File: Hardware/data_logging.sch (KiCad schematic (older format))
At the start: 8 parts, among them J5 DM3CS-SF, U7 W25Q128JVS

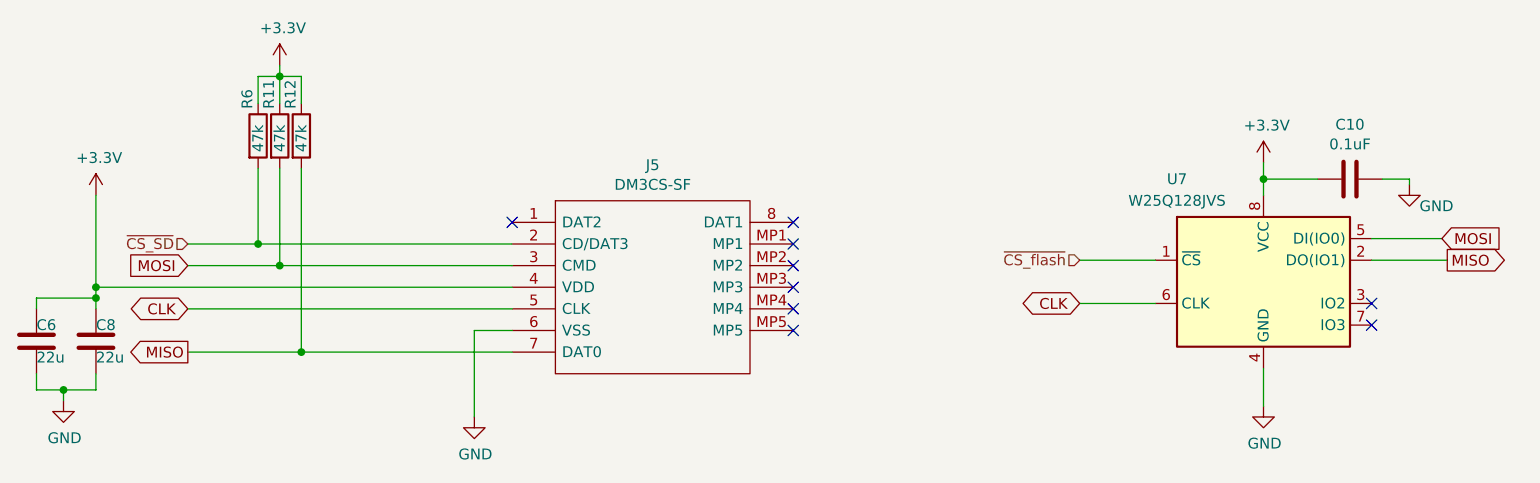
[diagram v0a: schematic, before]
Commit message: Update schematic, component placement
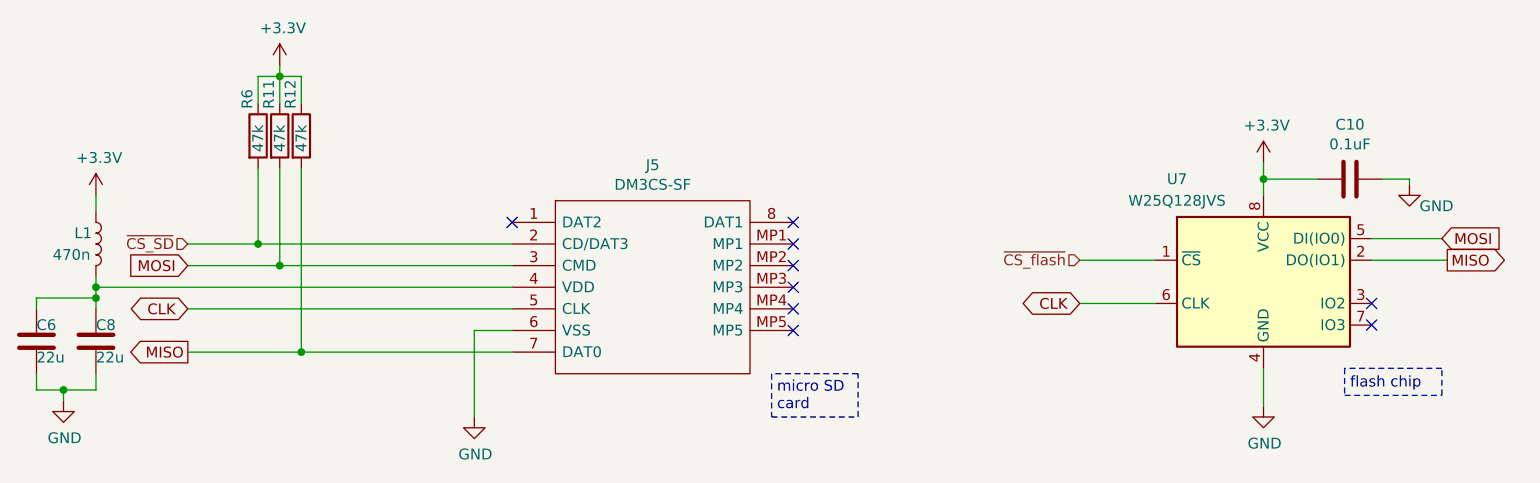
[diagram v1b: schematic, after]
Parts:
- added L1: 470n, Inductor_SMD:L_0603_1608Metric, symbol Device:L
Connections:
- net +3V3: now also L1.1; no longer C6.1, C8.1, J5.4 (VDD)
- new net: C6.1, C8.1, J5.4 (VDD), L1.2
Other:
- note added: "flash chip"
- note added: "micro SD \ncard"
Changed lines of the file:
@@
 	1    0    0    -1
 $EndComp
-Connection ~ 2825 3850
 Wire Wire Line
 	2550 3950 2550 3900
@@
 NoConn ~ 6050 3550
 NoConn ~ 4750 3550
-Wire Wire Line
-	2825 3425 2825 3850
 Text HLabel 7375 3725 0    50   Input ~ 0
 ~CS_flash
@@
 Text GLabel 9075 3725 2    50   Output ~ 0
 MISO
+$Comp
+L Device:L L1
+U 1 1 61194198
+P 2825 3650
+F 0 "L1" H 2725 3700 50  0000 L CNN
+F 1 "470n " H 2625 3600 50  0000 L CNN
+F 2 "Inductor_SMD:L_0603_1608Metric" H 2825 3650 50  0001 C CNN
+F 3 "~" H 2825 3650 50  0001 C CNN
+	1    2825 3650
+	1    0    0    -1
+$EndComp
+Wire Wire Line
+	2825 3800 2825 3850
+Connection ~ 2825 3850
+Wire Wire Line
+	2825 3425 2825 3500
+Text Notes 8625 4325 0    50   ~ 0
+flash chip
+Text Notes 5975 4425 0    50   ~ 0
+micro SD \ncard
+Wire Notes Line
+	5950 4450 6350 4450
+Wire Notes Line
+	6350 4450 6350 4250
+Wire Notes Line
+	6350 4250 5950 4250
+Wire Notes Line
+	5950 4250 5950 4450
+Wire Notes Line
+	8600 4225 8600 4350
+Wire Notes Line
+	8600 4350 9050 4350
+Wire Notes Line
+	9050 4350 9050 4225
+Wire Notes Line
+	9050 4225 8600 4225
 $EndSCHEMATC

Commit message: Change regulator diode footprint, update routing
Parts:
- J5: MANUFACTURER (none) -> HRS(Hirose)
- U7: MANUFACTURER (none) -> Winbond; Manufacturer_Part_Number (none) -> W25Q128JVSIQ
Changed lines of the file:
@@
 F 2 "Package_SO:SOIC-8_5.23x5.23mm_P1.27mm" H 8225 3825 50  0001 C CNN
 F 3 "http://www.winbond.com/resource-files/w25q128jv_dtr%20revc%2003272018%20plus.pdf" H 8225 3825 50  0001 C CNN
+F 4 "	Winbond" H 8225 3825 50  0001 C CNN "MANUFACTURER"
+F 5 "W25Q128JVSIQ" H 8225 3825 50  0001 C CNN "Manufacturer_Part_Number"
 	1    8225 3825
 	1    0    0    -1
@@
 F 10 "" H 5900 2850 50  0001 L CNN "Arrow Part Number"
 F 11 "" H 5900 2750 50  0001 L CNN "Arrow Price/Stock"
+F 12 "HRS(Hirose)" H 4750 3550 50  0001 C CNN "MANUFACTURER"
 	1    4750 3550
 	1    0    0    -1
